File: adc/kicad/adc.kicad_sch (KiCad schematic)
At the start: 70 parts, among them J1 Conn_01x05_Pin, J2 Conn_01x06_Pin, J3 Conn_01x05_Pin, J4 Conn_01x03_Pin, U1 ESD5344D-TP, U2 ESD5344D-TP, U3 ADS1261B, U4 ESD5344D-TP, U5 TPS7A2050PDBVR, U6 TPS61252DSG, U7 XC6206P332MR

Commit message: More progress on the ADC schematic.
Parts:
- removed J1, J3: Conn_01x05_Pin, adc:PinHeader_1x05_P2.54mm_Vertical, symbol Connector:Conn_01x05_Pin
- removed J4: Conn_01x03_Pin, adc:PinHeader_1x02_P2.54mm_Vertical, symbol Connector:Conn_01x02_Pin
- removed R11, R12, R8, R9: 47R, Resistor_SMD:R_0402_1005Metric, symbol Device:R_Small_US
- removed R13, R20: 51K, Resistor_SMD:R_0402_1005Metric, symbol Device:R_Small_US
- removed U1: ESD5344D-TP, common:Diodes_UDFN-10_1.0x2.5mm_P0.5mm, symbol common:ESD5344D
- added J5: pcie_98, common:PCIE_98_CARD, symbol common:PCIE_98_EDGE
- J2: footprint adc:PinHeader_1x06_P2.54mm_Vertical -> adc:PinHeader_1x04_P2.54mm_Vertical; symbol Connector:Conn_01x06_Pin -> Connector:Conn_01x04_Pin
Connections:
- net +3V3: now also U3.7 (PWDN_N), U3.8 (RESET_N)
- net +5VA: now also J2.4 (Pin_4); no longer J2.6 (Pin_6)
- net GNDD: now also U3.9 (START), J5.A1 (Pin_a1), J5.A2 (Pin_a2), J5.A3 (Pin_a3), J5.A4 (Pin_a4)
- net at J2.2 (Pin_2), R19.1: now also U2.2 (D2); no longer U2.1 (D1)
- net PB14: now reaches R18.1, U4.1 (D1)
- net PB14: now also J5.B14 (Pin_b14)
- net PA5: now reaches R17.1, U4.2 (D2)
- net PA5: now also J5.B28 (Pin_b28)
- net PA6: now reaches R16.1, U4.4 (D3)
- net PA6: now also J5.B21 (Pin_b21)
- net PA7: now reaches R15.1, U4.5 (D4)
- net PA7: now also J5.A27 (Pin_a27)
- net +5VD: now reaches C17.2, C20.2, C25.2, C26.2, L1.1, U6.6 (EN), U6.8 (VIN), U7.3 (VIN)
- net +5VD: now also J5.B1 (Pin_b1), J5.B2 (Pin_b2), J5.B3 (Pin_b3), J5.B4 (Pin_b4)
- net at R5.1: now also R16.2, U3.14 (MISO); no longer U3.8 (RESET_N)
- net at J2.3 (Pin_3), R14.1: now also U2.1 (D1); no longer U2.2 (D2)
- net at R18.2, U3.10 (CS_N): now also R6.1
- now unconnected: R10.1, R3.1, U2.4 (D3), U2.5 (D4)
- no-connect marks 6 -> 9
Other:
- note added: "ADD INPUTS for two thermistors."
- note added: "Consider to have ratiometric measurement of the load cell."
- note added: "LOAD CELL"
- note added: "TODO: Add jumpers for two SPI channels."
- note added: "TODO: Should MOSI be pulled up or down?"
- note removed: "5V"
- note removed: "TODO: Add pullup to MISO (ADC Pin 14)"
- note removed: "TODO: Change CS pulldown to pullup."
- moved on the sheet: C1, C10, C11, C12, C13, C14, C15, C16, C17, C18, C19, C2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

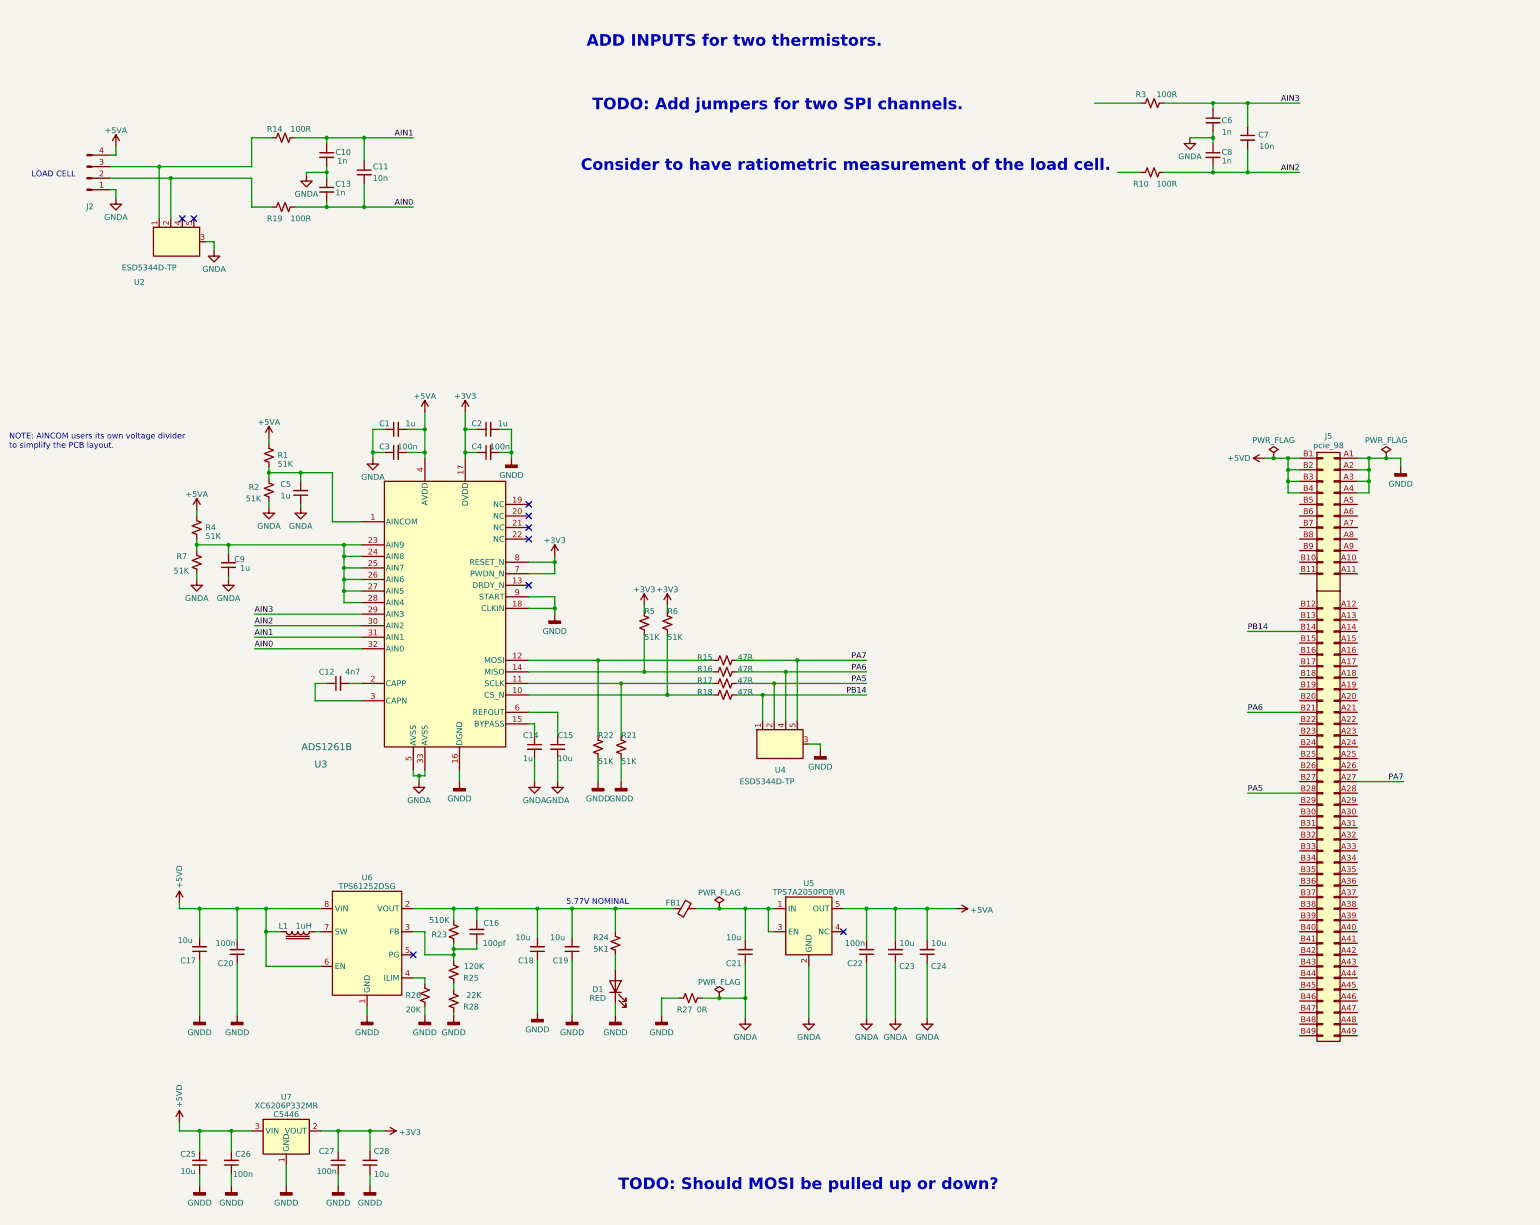
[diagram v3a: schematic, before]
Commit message: Minor schematic tweaks.
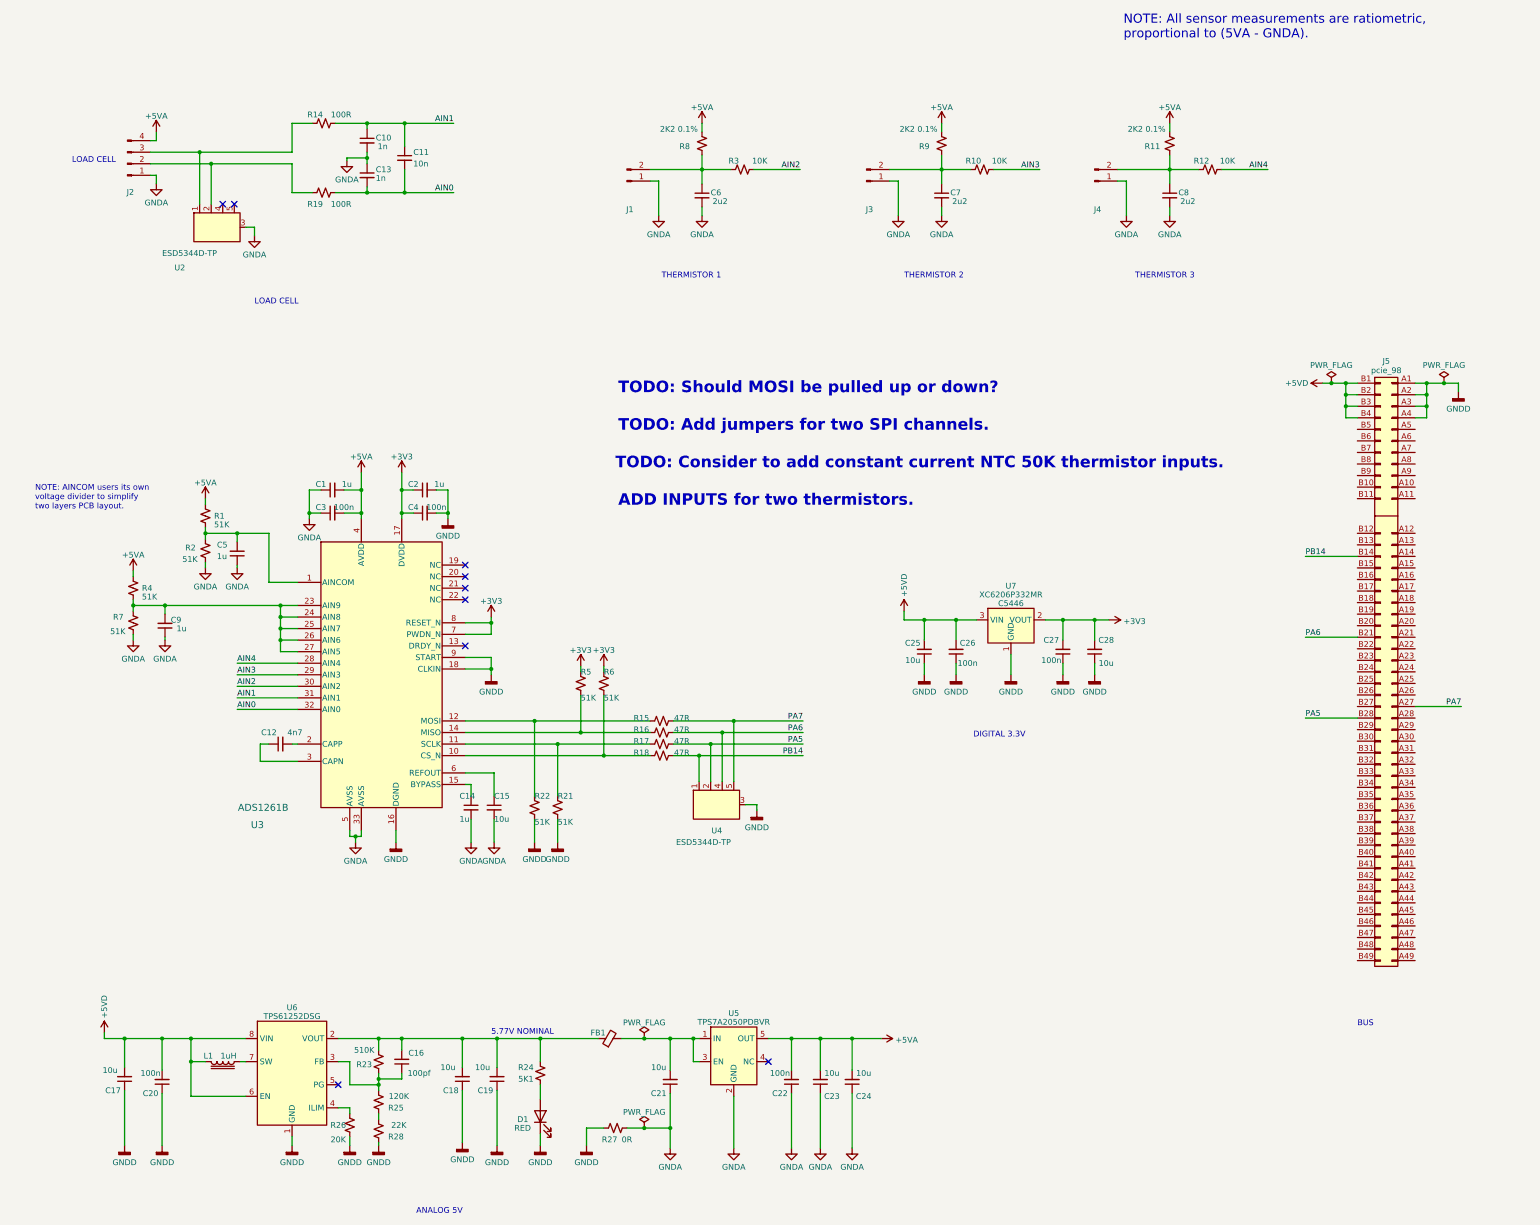
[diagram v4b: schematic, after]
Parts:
- added J1, J3, J4: Conn_01x02_Pin, symbol Connector:Conn_01x02_Pin
- added R11, R8, R9: 2K2 0.1%, Resistor_SMD:R_0402_1005Metric, symbol Device:R_Small_US
- added R12: 10K, Resistor_SMD:R_0402_1005Metric, symbol Device:R_Small_US
- C6, C8: value 1n -> 2u2
- C7: value 10n -> 2u2; LCSC C15195 -> C1523
- J2: value Conn_01x06_Pin -> Conn_01x04_Pin; footprint adc:PinHeader_1x04_P2.54mm_Vertical -> (none); LCSC DNP -> (none)
- R10, R3: value 100R -> 10K; LCSC C25076 -> (none)
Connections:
- net +5VA: now also R11.2, R8.2, R9.2
- net AIN2: now also R3.2; no longer C7.2, C8.2, R10.2
- net AIN3: now also R10.2; no longer C6.1, C7.1, R3.2
- net GNDA: now also C7.2, C8.2, J1.1 (Pin_1), J3.1 (Pin_1), J4.1 (Pin_1); no longer C8.1
- net at R10.1: now also C7.1, J3.2 (Pin_2), R9.1
- net at C9.2, R4.1, R7.2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: no longer U3.28 (AIN4)
- net at R3.1: now also C6.1, J1.2 (Pin_2), R8.1
- new net: C8.1, J4.2 (Pin_2), R11.1, R12.1
- new net AIN4: R12.2, U3.28 (AIN4)
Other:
- note added: "ANALOG 5V"
- note added: "BUS"
- note added: "DIGITAL 3.3V"
- note added: "NOTE: AINCOM users its own voltage divider to simplify two layers PCB layout."
- note added: "NOTE: All sensor measurements are ratiometric, proportional to (5VA - GNDA)."
- note added: "THERMISTOR 1"
- note added: "THERMISTOR 2"
- note added: "THERMISTOR 3"
- note added: "TODO: Consider to add constant current NTC 50K thermistor inputs."
- note removed: "Consider to have ratiometric measurement of the load cell."
- note removed: "NOTE: AINCOM users its own voltage divider to simplify the PCB layout."
- moved on the sheet: C1, C10, C11, C12, C13, C14, C15, C16, C17, C18, C19, C2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

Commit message: Updated the input capacitor values of the ADC schematic (based on SPICE simulation)
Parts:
- C10, C13: value 1n -> 33n; LCSC C1523 -> (none)
- C11: value 10n -> 330n; LCSC C15195 -> (none)
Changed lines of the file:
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@@
       (effects (font (size 1.27 1.27)) (justify left))
     )
-    (property "Value" "1n" (at 101.6 53.975 0)
+    (property "Value" "33n" (at 101.6 53.975 0)
       (effects (font (size 1.27 1.27)) (justify left))
     )
@@
       (effects (font (size 1.27 1.27)) hide)
     )
-    (property "LCSC" "C1523" (at 99.695 53.34 0)
+    (property "LCSC" "" (at 99.695 53.34 0)
       (effects (font (size 1.27 1.27)) hide)
     )
@@
       (effects (font (size 1.27 1.27)) (justify left))
     )
-    (property "Value" "1n" (at 102.0191 47.0036 0)
+    (property "Value" "33n" (at 102.0191 47.0036 0)
       (effects (font (size 1.27 1.27)) (justify left))
     )
@@
       (effects (font (size 1.27 1.27)) hide)
     )
-    (property "LCSC" "C1523" (at 99.695 45.72 0)
+    (property "LCSC" "" (at 99.695 45.72 0)
       (effects (font (size 1.27 1.27)) hide)
     )
@@
       (effects (font (size 1.27 1.27)) (justify left))
     )
-    (property "Value" "10n" (at 109.855 50.8 0)
+    (property "Value" "330n" (at 109.855 50.8 0)
       (effects (font (size 1.27 1.27)) (justify left))
     )
@@
       (effects (font (size 1.27 1.27)) hide)
     )
-    (property "LCSC" "C15195" (at 107.95 49.53 0)
-      (effects (font (size 1.27 1.27)) hide)
-    )
+    (property "LCSC" "" (at 107.95 49.53 0)
+      (effects (font (size 1.27 1.27)) hide)
+    )

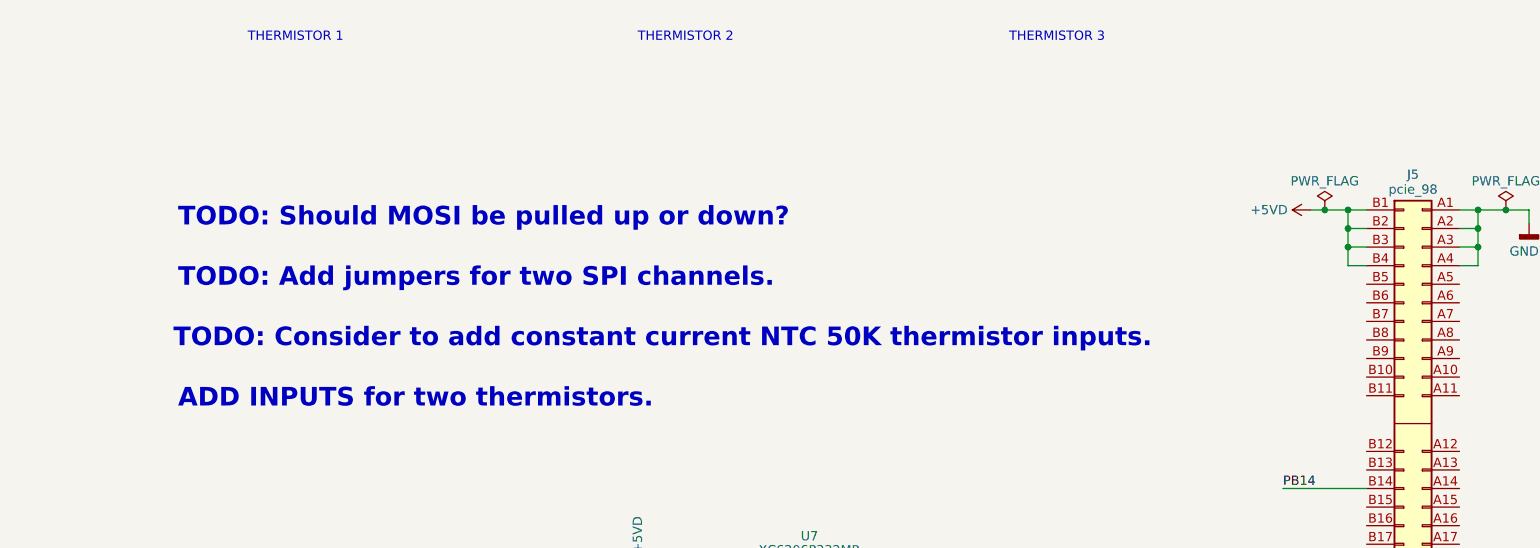
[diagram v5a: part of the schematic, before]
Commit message: Minor tweak of the ADC schematic.
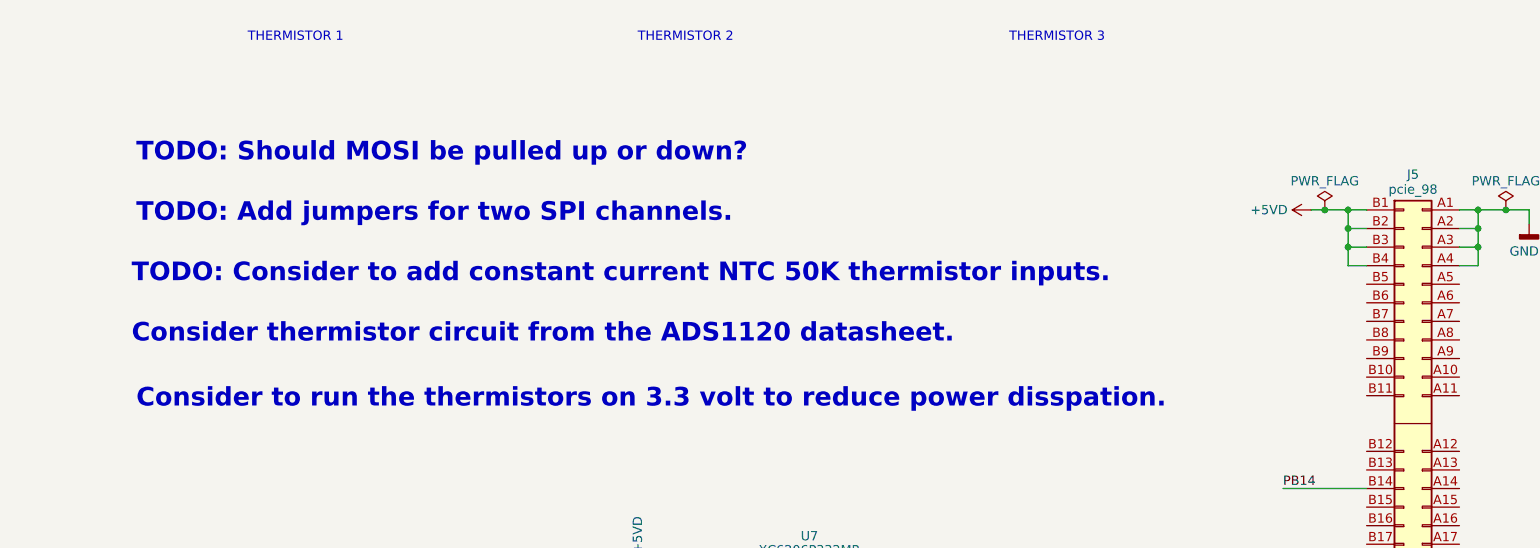
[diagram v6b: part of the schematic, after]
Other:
- note added: "Consider thermistor circuit from the ADS1120 datasheet."
- note added: "Consider to run the thermistors on 3.3 volt to reduce power disspation."
- note removed: "ADD INPUTS for two thermistors."
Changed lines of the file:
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@@
     (stroke (width 0) (type default))
   )
-  (text "TODO: Should MOSI be pulled up or down?" (at 154.94 101.6 0)
+  (text "TODO: Should MOSI be pulled up or down?" (at 149.225 92.71 0)
+    (effects (font (size 2.54 2.54) (thickness 0.508) bold (color 255 0 0 1)) (justify left bottom))
+  )
+  (text "Consider to run the thermistors on 3.3 volt to reduce power disspation."
+    (at 149.225 126.365 0)
     (effects (font (size 2.54 2.54) (thickness 0.508) bold (color 255 0 0 1)) (justify left bottom))
   )
   (text "TODO: Consider to add constant current NTC 50K thermistor inputs."
-    (at 154.305 118.11 0)
+    (at 148.59 109.22 0)
     (effects (font (size 2.54 2.54) (thickness 0.508) bold (color 255 0 0 1)) (justify left bottom))
   )
@@
     (effects (font (size 1.27 1.27)) (justify right bottom))
   )
-  (text "TODO: Add jumpers for two SPI channels." (at 154.94 109.855 0)
+  (text "TODO: Add jumpers for two SPI channels." (at 149.225 100.965 0)
+    (effects (font (size 2.54 2.54) (thickness 0.508) bold (color 255 0 0 1)) (justify left bottom))
+  )
+  (text "Consider thermistor circuit from the ADS1120 datasheet."
+    (at 148.59 117.475 0)
     (effects (font (size 2.54 2.54) (thickness 0.508) bold (color 255 0 0 1)) (justify left bottom))
   )
@@
     (effects (font (size 1.27 1.27)) (justify left bottom))
   )
-  (text "ADD INPUTS for two thermistors." (at 154.94 126.365 0)
-    (effects (font (size 2.54 2.54) (thickness 0.508) bold (color 255 0 0 1)) (justify left bottom))
-  )
   (text "LOAD CELL" (at 74.93 81.915 0)
